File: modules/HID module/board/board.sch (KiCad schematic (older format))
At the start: 40 parts, among them J1 USB_B, J2 Conn_01x06_Female, J3 Conn_02x12_Odd_Even, J4 Conn_02x12_Odd_Even, SW1 SW_Push, SW2 SW_Push, SW3 SW_Push, SW4 SW_Push, U1 AMS1117-3.3, U2 ATmega32U4-AU, U3 ESP32-WROOM-32D, Y1 16MHz

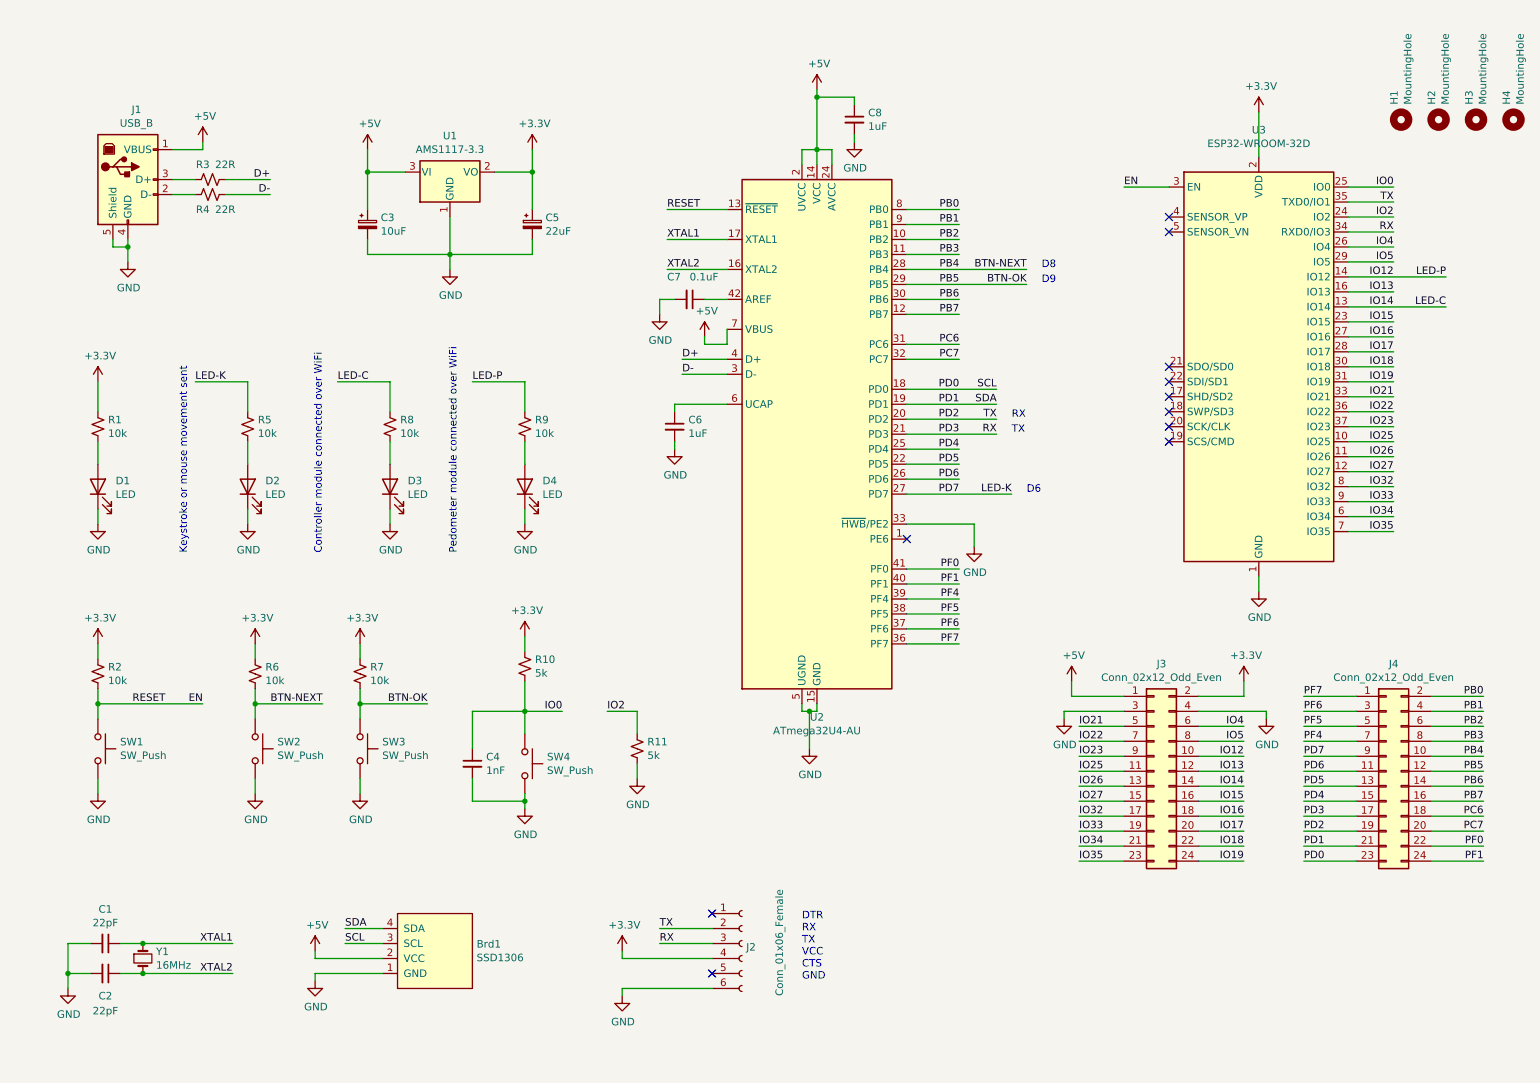
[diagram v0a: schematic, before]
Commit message: HID module: Schematic and PCB layout
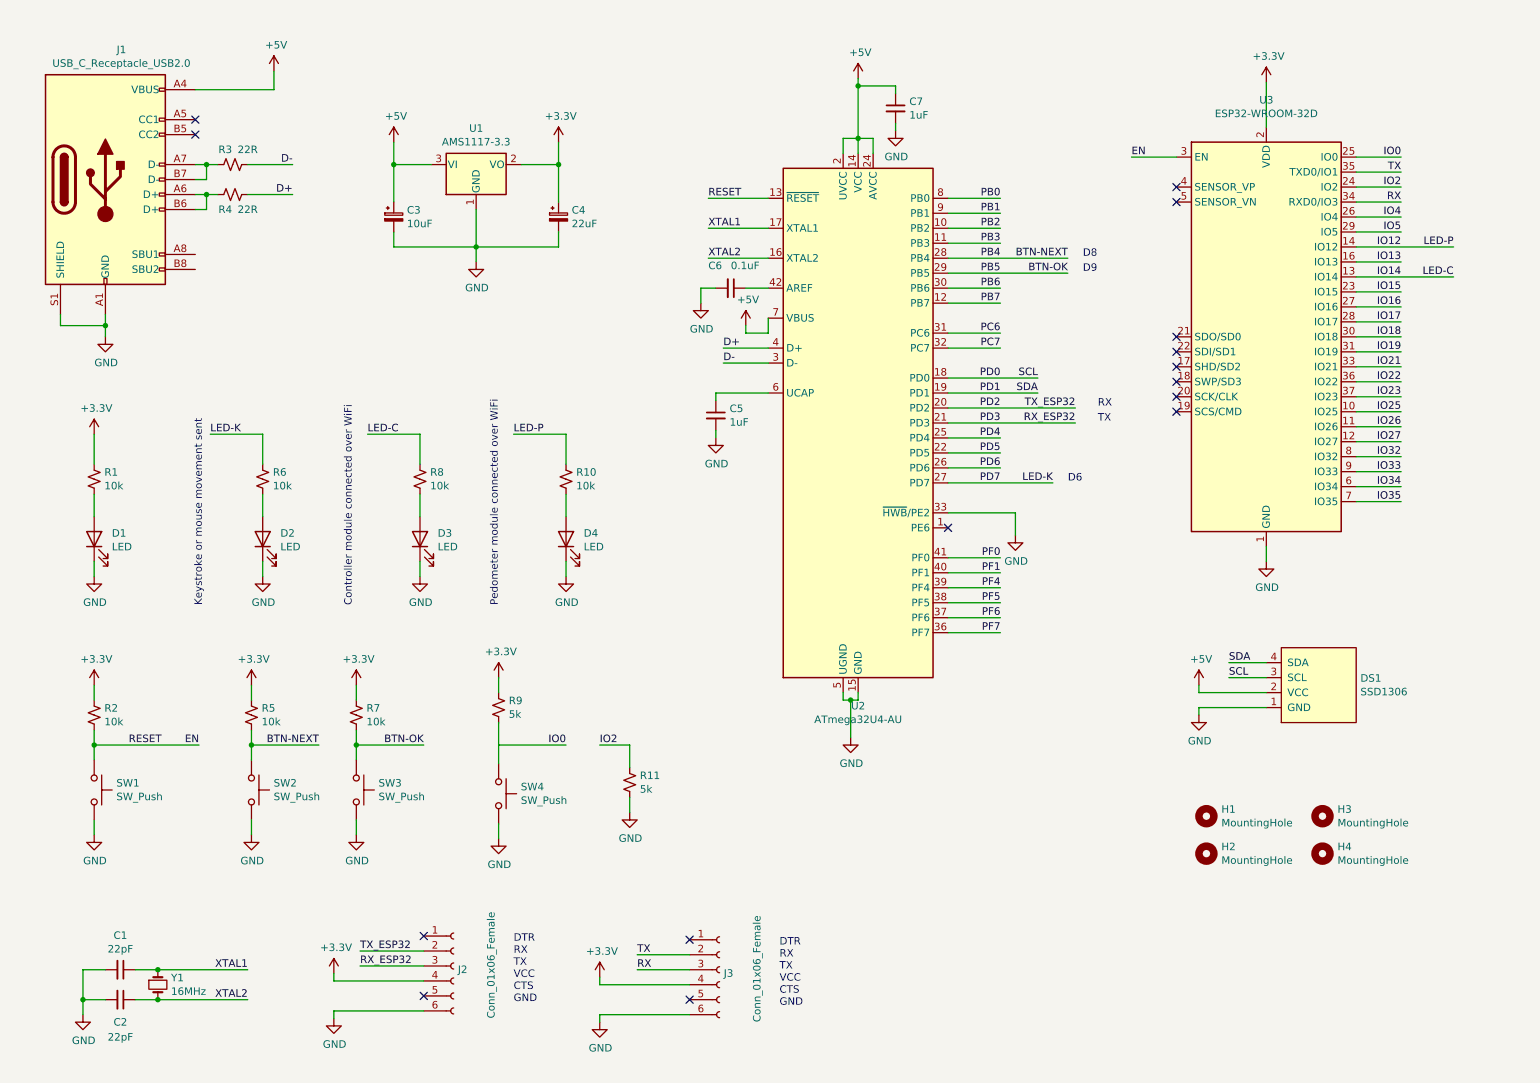
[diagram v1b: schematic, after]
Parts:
- removed C4: 1nF, Capacitor_SMD:C_0805_2012Metric_Pad1.18x1.45mm_HandSolder, symbol Device:C_Small
- removed J1: USB_B, Connector_USB:USB_B_OST_USB-B1HSxx_Horizontal, symbol Connector:USB_B
- removed J3, J4: Conn_02x12_Odd_Even, Connector_PinSocket_2.54mm:PinSocket_2x12_P2.54mm_Vertical_SMD, symbol Connector_Generic:Conn_02x12_Odd_Even
- added J1: USB_C_Receptacle_USB2.0, Connector_USB:USB_C_Receptacle_HRO_TYPE-C-31-M-12, symbol Connector:USB_C_Receptacle_USB2.0
- added J3: Conn_01x06_Female, Board:SolderWire_1x06_P2.54mm, symbol Connector:Conn_01x06_Female
- DS1: renamed from Brd1; footprint Connector_PinSocket_2.54mm:PinSocket_1x04_P2.54mm_Vertical -> Board:128x64OLED
- H1, H2, H3, H4: footprint MountingHole:MountingHole_3.2mm_M3 -> MountingHole:MountingHole_2.2mm_M2
- J2: footprint Connector_PinSocket_2.54mm:PinSocket_1x06_P2.54mm_Vertical -> Board:SolderWire_1x06_P2.54mm
- SW1, SW4: footprint Button_Switch_SMD:SW_SPST_Omron_B3FS-105xP -> Button_Switch_SMD:SW_SPST_B3U-1000P
- SW2, SW3: footprint Button_Switch_SMD:SW_SPST_Omron_B3FS-105xP -> Button_Switch_SMD:SW_SPST_Omron_B3FS-100xP
- Y1: footprint Crystal:Crystal_HC49-4H_Vertical -> Crystal:Crystal_SMD_HC49-SD
- renumbered C5 to C4, C6 to C5, C7 to C6, C8 to C7, R9 to R10, R6 to R5, R5 to R6, R10 to R9
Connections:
- net +3V3: now also J3.4 (Pin_4)
- net +5V: now also J1.A4 (VBUS), J1.A9 (VBUS), J1.B4 (VBUS), J1.B9 (VBUS)
- net D+: now also R4.1; no longer R3.1
- net D-: now also R3.1; no longer R4.1
- net GND: now also J1.A1 (GND), J1.A12 (GND), J1.B1 (GND), J1.B12 (GND), J1.S1 (SHIELD), J3.6 (Pin_6)
- net IO0: no longer R9.2, SW4.1
- net PD2: no longer U3.35 (TXD0/IO1)
- net PD3: no longer U3.34 (RXD0/IO3)
- net at R3.2: now also J1.A7 (D-), J1.B7 (D-)
- net at R4.2: now also J1.A6 (D+), J1.B6 (D+)
- new net: R9.2, SW4.1
- new net RX: J3.3 (Pin_3), U3.34 (RXD0/IO3)
- new net TX: J3.2 (Pin_2), U3.35 (TXD0/IO1)
- no-connect marks 11 -> 15
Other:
- moved on the sheet: C1, C2, C3, C4, C5, C6, C7, D1, D2, D3, D4, DS1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

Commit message: HID module: PCB complete
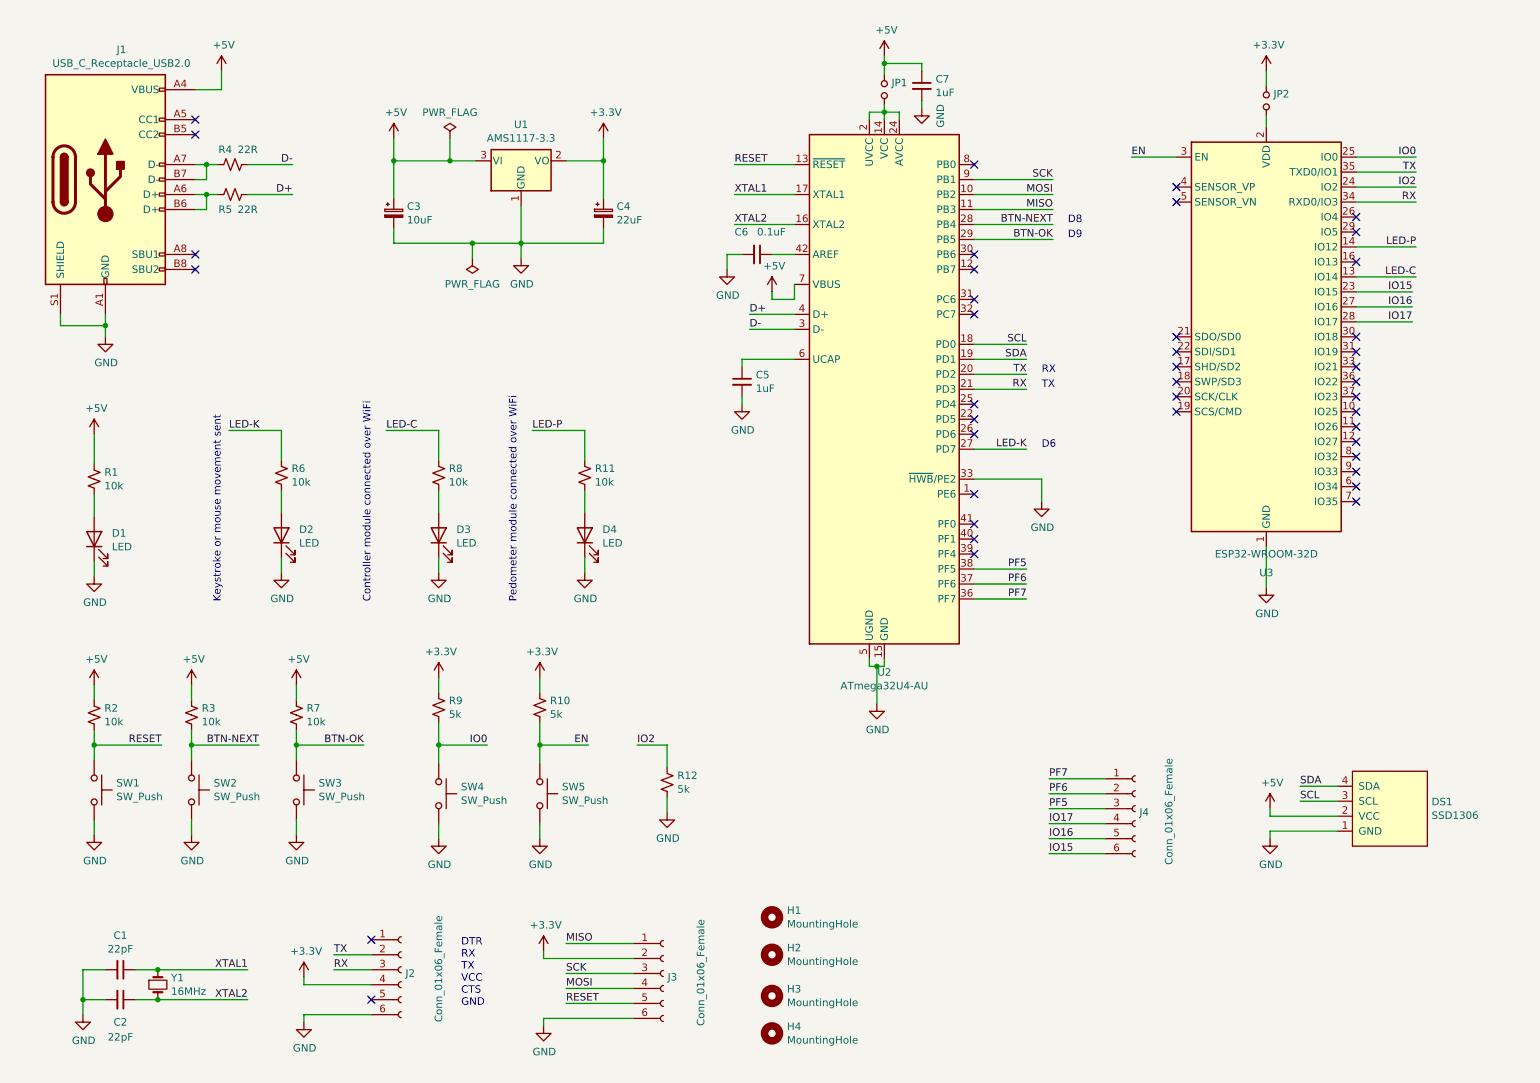
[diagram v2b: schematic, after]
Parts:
- added J4: Conn_01x06_Female, Board:SolderWire_1x06_P2.54mm, symbol Connector:Conn_01x06_Female
- added JP1, JP2: Jumper_NO_Small, Jumper:SolderJumper-2_P1.3mm_Open_RoundedPad1.0x1.5mm, symbol Device:Jumper_NO_Small
- added R10: 5k, Resistor_SMD:R_0805_2012Metric_Pad1.20x1.40mm_HandSolder, symbol Device:R_Small_US
- added SW5: SW_Push, Button_Switch_SMD:SW_SPST_B3U-1000P, symbol Switch:SW_Push
- renumbered R10 to R11, R11 to R12, R5 to R3, R3 to R4, R4 to R5
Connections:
- net PB3 is gone; now on net MISO: U2.11 (PB3)
- net PD2 is gone; now on net TX: J2.2 (Pin_2), U2.20 (PD2)
- net PD3 is gone; now on net RX: J2.3 (Pin_3), U2.21 (PD3)
- net +3V3: now also J3.2 (Pin_2), JP2.1, R10.1; no longer J3.4 (Pin_4), R1.1, R2.1, R3.1, R7.1, U3.2 (VDD)
- net +5V: now also R1.1, R2.1, R3.1, R7.1, JP1.1; no longer U2.14 (VCC), U2.2 (UVCC), U2.24 (AVCC), U2.34 (VCC), U2.44 (AVCC)
- net EN: now also R10.2, SW5.1; no longer R2.2, SW1.1, U2.13 (~RESET)
- net GND: now also SW5.2
- net IO0: now also R9.2, SW4.1
- net IO15: now also J4.6 (Pin_6)
- net IO16: now also J4.5 (Pin_5)
- net IO17: now also J4.4 (Pin_4)
- net PF5: now also J4.3 (Pin_3)
- net PF6: now also J4.2 (Pin_2)
- net PF7: now also J4.1 (Pin_1)
- net RX: no longer J3.3 (Pin_3)
- net TX: no longer J3.2 (Pin_2)
- net MISO: now reaches J3.1 (Pin_1)
- net RESET: now reaches J3.5 (Pin_5)
- net RESET: now also R2.2, SW1.1, U2.13 (~RESET)
- net IO12 renamed LED-P
- net IO13: no longer names the net of U3.16 (IO13)
- net IO14 renamed LED-C
- net IO18: no longer names the net of U3.30 (IO18)
- net IO19: no longer names the net of U3.31 (IO19)
- net IO21: no longer names the net of U3.33 (IO21)
- net IO22: no longer names the net of U3.36 (IO22)
- net IO23: no longer names the net of U3.37 (IO23)
- net IO25: no longer names the net of U3.10 (IO25)
- net IO26: no longer names the net of U3.11 (IO26)
- net IO27: no longer names the net of U3.12 (IO27)
- net IO32: no longer names the net of U3.8 (IO32)
- net IO33: no longer names the net of U3.9 (IO33)
- net IO34: no longer names the net of U3.6 (IO34)
- net IO35: no longer names the net of U3.7 (IO35)
- net IO4: no longer names the net of U3.26 (IO4)
- net IO5: no longer names the net of U3.29 (IO5)
- net PB0: no longer names the net of U2.8 (PB0)
- net PB1 renamed SCK
- net SCK: now also J3.3 (Pin_3)
- net PB2 renamed MOSI
- net MOSI: now also J3.4 (Pin_4)
- net PB6: no longer names the net of U2.30 (PB6)
- net PB7: no longer names the net of U2.12 (PB7)
- net PC6: no longer names the net of U2.31 (PC6)
- net PC7: no longer names the net of U2.32 (PC7)
- net PD0 renamed SCL
- net PD1 renamed SDA
- net PD4: no longer names the net of U2.25 (PD4)
- net PD5: no longer names the net of U2.22 (PD5)
- net PD6: no longer names the net of U2.26 (PD6)
- net PF0: no longer names the net of U2.41 (PF0)
- net PF1: no longer names the net of U2.40 (PF1)
- net PF4: no longer names the net of U2.39 (PF4)
- new net: JP1.2, U2.14 (VCC), U2.2 (UVCC), U2.24 (AVCC), U2.34 (VCC), U2.44 (AVCC)
- new net: JP2.2, U3.2 (VDD)
- no-connect marks 15 -> 41
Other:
- moved on the sheet: C3, C4, C5, C6, C7, D2, D3, D4, DS1, H1, H2, H3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

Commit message: HID module: PCB modular
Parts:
- R4, R5: footprint Resistor_SMD:R_0805_2012Metric_Pad1.20x1.40mm_HandSolder -> Resistor_SMD:R_0603_1608Metric
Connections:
- net _D-: now reaches J1.A7 (D-), J1.B7 (D-), R4.2
- net _D+: now reaches J1.A6 (D+), J1.B6 (D+), R5.2
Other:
- moved on the sheet: C1, C2, C5, C6, C7, D1, D2, D3, D4, DS1, H1, H2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

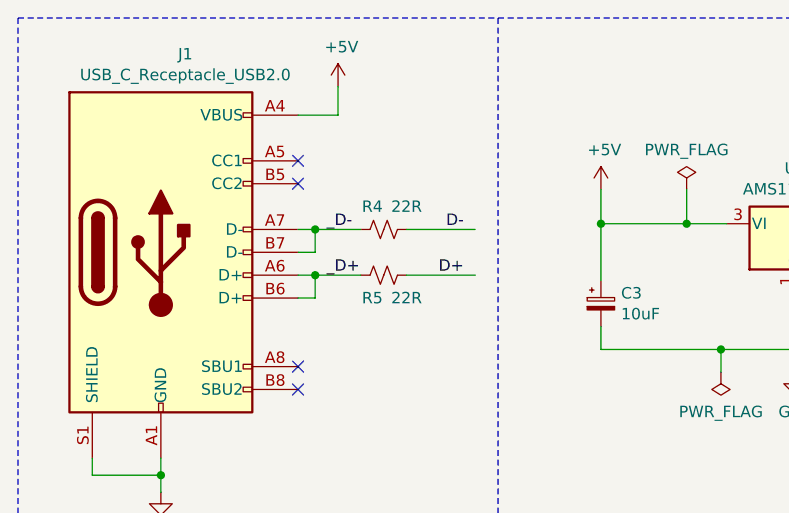
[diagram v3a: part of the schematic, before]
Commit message: PCB: USB receptacle moved closer to PCB edge
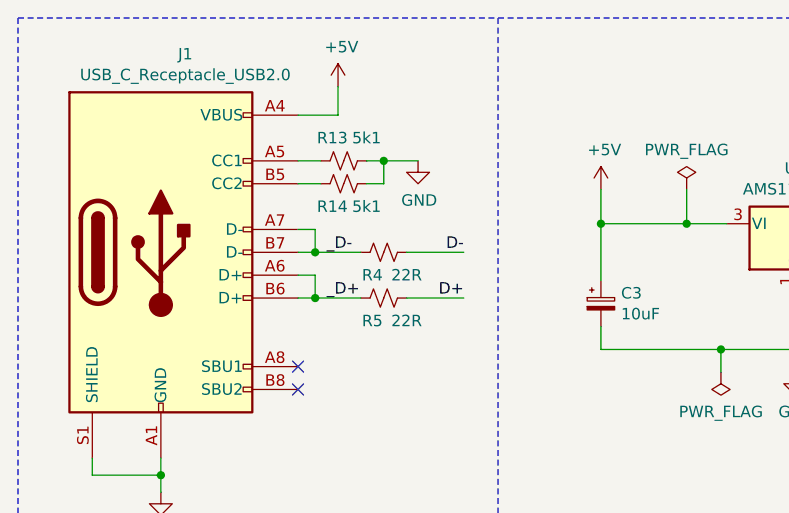
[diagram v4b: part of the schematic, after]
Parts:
- added R13, R14: 5k1, Resistor_SMD:R_0603_1608Metric, symbol Device:R_Small_US
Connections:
- net GND: now also R13.1, R14.1
- net at J1.A5 (CC1): now also R13.2
- net at J1.B5 (CC2): now also R14.2
- no-connect marks 41 -> 39
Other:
- moved on the sheet: R4, R5
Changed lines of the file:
@@
 	1    0    0    -1
 $EndComp
-Text Label 2825 1750 2    50   ~ 0
+Text Label 2825 1850 2    50   ~ 0
 D+
-Text Label 2825 1550 2    50   ~ 0
+Text Label 2825 1650 2    50   ~ 0
 D-
 Wire Wire Line
@@
 Wire Wire Line
 	1500 2625 1500 2700
-$Comp
-L Connector:USB_C_Receptacle_USB2.0 J1
-U 1 1 6230F664
-P 1500 1650
-F 0 "J1" H 1607 2517 50  0000 C CNN
-F 1 "USB_C_Receptacle_USB2.0" H 1607 2426 50  0000 C CNN
-F 2 "Connector_USB:USB_C_Receptacle_HRO_TYPE-C-31-M-12" H 1650 1650 50  0001 C CNN
-F 3 "https://www.usb.org/sites/default/files/documents/usb_type-c.zip" H 1650 1650 50  0001 C CNN
-	1    1500 1650
-	1    0    0    -1
-$EndComp
 Wire Wire Line
 	2100 1550 2175 1550
@@
 	2100 1750 2175 1750
 Wire Wire Line
-	2175 1550 2175 1650
-Wire Wire Line
 	2175 1650 2100 1650
-Wire Wire Line
-	2175 1750 2175 1850
 Wire Wire Line
 	2175 1850 2100 1850
@@
 	1    0    0    -1
 $EndComp
-NoConn ~ 2100 1250
-NoConn ~ 2100 1350
 $Comp
 L Regulator_Linear:AMS1117-3.3 U1
@@
 L Device:R_Small_US R5
 U 1 1 619AA856
-P 2475 1750
-F 0 "R5" V 2575 1700 50  0000 C CNN
-F 1 "22R" V 2575 1850 50  0000 C CNN
-F 2 "Resistor_SMD:R_0603_1608Metric" H 2475 1750 50  0001 C CNN
-F 3 "~" H 2475 1750 50  0001 C CNN
-	1    2475 1750
+P 2475 1850
+F 0 "R5" V 2575 1800 50  0000 C CNN
+F 1 "22R" V 2575 1950 50  0000 C CNN
+F 2 "Resistor_SMD:R_0603_1608Metric" H 2475 1850 50  0001 C CNN
+F 3 "~" H 2475 1850 50  0001 C CNN
+	1    2475 1850
 	0    1    1    0
 $EndComp
-Wire Wire Line
-	2575 1750 2875 1750
-Wire Wire Line
-	2875 1550 2575 1550
-Text Label 2225 1550 0    50   ~ 0
+Text Label 2225 1650 0    50   ~ 0
 _D-
 $Comp
 L Device:R_Small_US R4
 U 1 1 619A9A9A
-P 2475 1550
-F 0 "R4" V 2375 1500 50  0000 C CNN
-F 1 "22R" V 2375 1650 50  0000 C CNN
-F 2 "Resistor_SMD:R_0603_1608Metric" H 2475 1550 50  0001 C CNN
-F 3 "~" H 2475 1550 50  0001 C CNN
-	1    2475 1550
+P 2475 1650
+F 0 "R4" V 2575 1600 50  0000 C CNN
+F 1 "22R" V 2575 1750 50  0000 C CNN
+F 2 "Resistor_SMD:R_0603_1608Metric" H 2475 1650 50  0001 C CNN
+F 3 "~" H 2475 1650 50  0001 C CNN
+	1    2475 1650
 	0    1    1    0
 $EndComp
 Wire Wire Line
-	2175 1550 2375 1550
-Connection ~ 2175 1550
-Wire Wire Line
-	2175 1750 2375 1750
-Connection ~ 2175 1750
-Text Label 2225 1750 0    50   ~ 0
+	2175 1650 2375 1650
+Wire Wire Line
+	2175 1850 2375 1850
+Text Label 2225 1850 0    50   ~ 0
 _D+
+$Comp
+L Connector:USB_C_Receptacle_USB2.0 J1
+U 1 1 6230F664
+P 1500 1650
+F 0 "J1" H 1607 2517 50  0000 C CNN
+F 1 "USB_C_Receptacle_USB2.0" H 1607 2426 50  0000 C CNN
+F 2 "Connector_USB:USB_C_Receptacle_HRO_TYPE-C-31-M-12" H 1650 1650 50  0001 C CNN
+F 3 "https://www.usb.org/sites/default/files/documents/usb_type-c.zip" H 1650 1650 50  0001 C CNN
+	1    1500 1650
+	1    0    0    -1
+$EndComp
+$Comp
+L Device:R_Small_US R13
+U 1 1 63D7B37D
+P 2300 1250
+F 0 "R13" V 2200 1200 50  0000 C CNN
+F 1 "5k1" V 2200 1350 50  0000 C CNN
+F 2 "Resistor_SMD:R_0603_1608Metric" H 2300 1250 50  0001 C CNN
+F 3 "~" H 2300 1250 50  0001 C CNN
+	1    2300 1250
+	0    1    1    0
+$EndComp
+$Comp
+L power:GND #PWR038
+U 1 1 63D7CAEF
+P 2625 1250
+F 0 "#PWR038" H 2625 1000 50  0001 C CNN
+F 1 "GND" H 2630 1077 50  0000 C CNN
+F 2 "" H 2625 1250 50  0001 C CNN
+F 3 "" H 2625 1250 50  0001 C CNN
+	1    2625 1250
+	1    0    0    -1
+$EndComp
+$Comp
+L Device:R_Small_US R14
+U 1 1 63D7D4EA
+P 2300 1350
+F 0 "R14" V 2400 1300 50  0000 C CNN
+F 1 "5k1" V 2400 1450 50  0000 C CNN
+F 2 "Resistor_SMD:R_0603_1608Metric" H 2300 1350 50  0001 C CNN
+F 3 "~" H 2300 1350 50  0001 C CNN
+	1    2300 1350
+	0    1    1    0
+$EndComp
+Wire Wire Line
+	2100 1250 2200 1250
+Wire Wire Line
+	2200 1350 2100 1350
+Wire Wire Line
+	2400 1350 2475 1350
+Wire Wire Line
+	2475 1350 2475 1250
+Wire Wire Line
+	2475 1250 2400 1250
+Wire Wire Line
+	2475 1250 2625 1250
+Connection ~ 2475 1250
+Wire Wire Line
+	2575 1650 2825 1650
+Wire Wire Line
+	2825 1850 2575 1850
+Connection ~ 2175 1650
+Connection ~ 2175 1850
+Wire Wire Line
+	2175 1550 2175 1650
+Wire Wire Line
+	2175 1750 2175 1850
 $EndSCHEMATC
